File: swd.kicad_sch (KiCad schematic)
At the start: 3 parts, among them J2 ARM JTAG, U1 STM32H753ZIT6

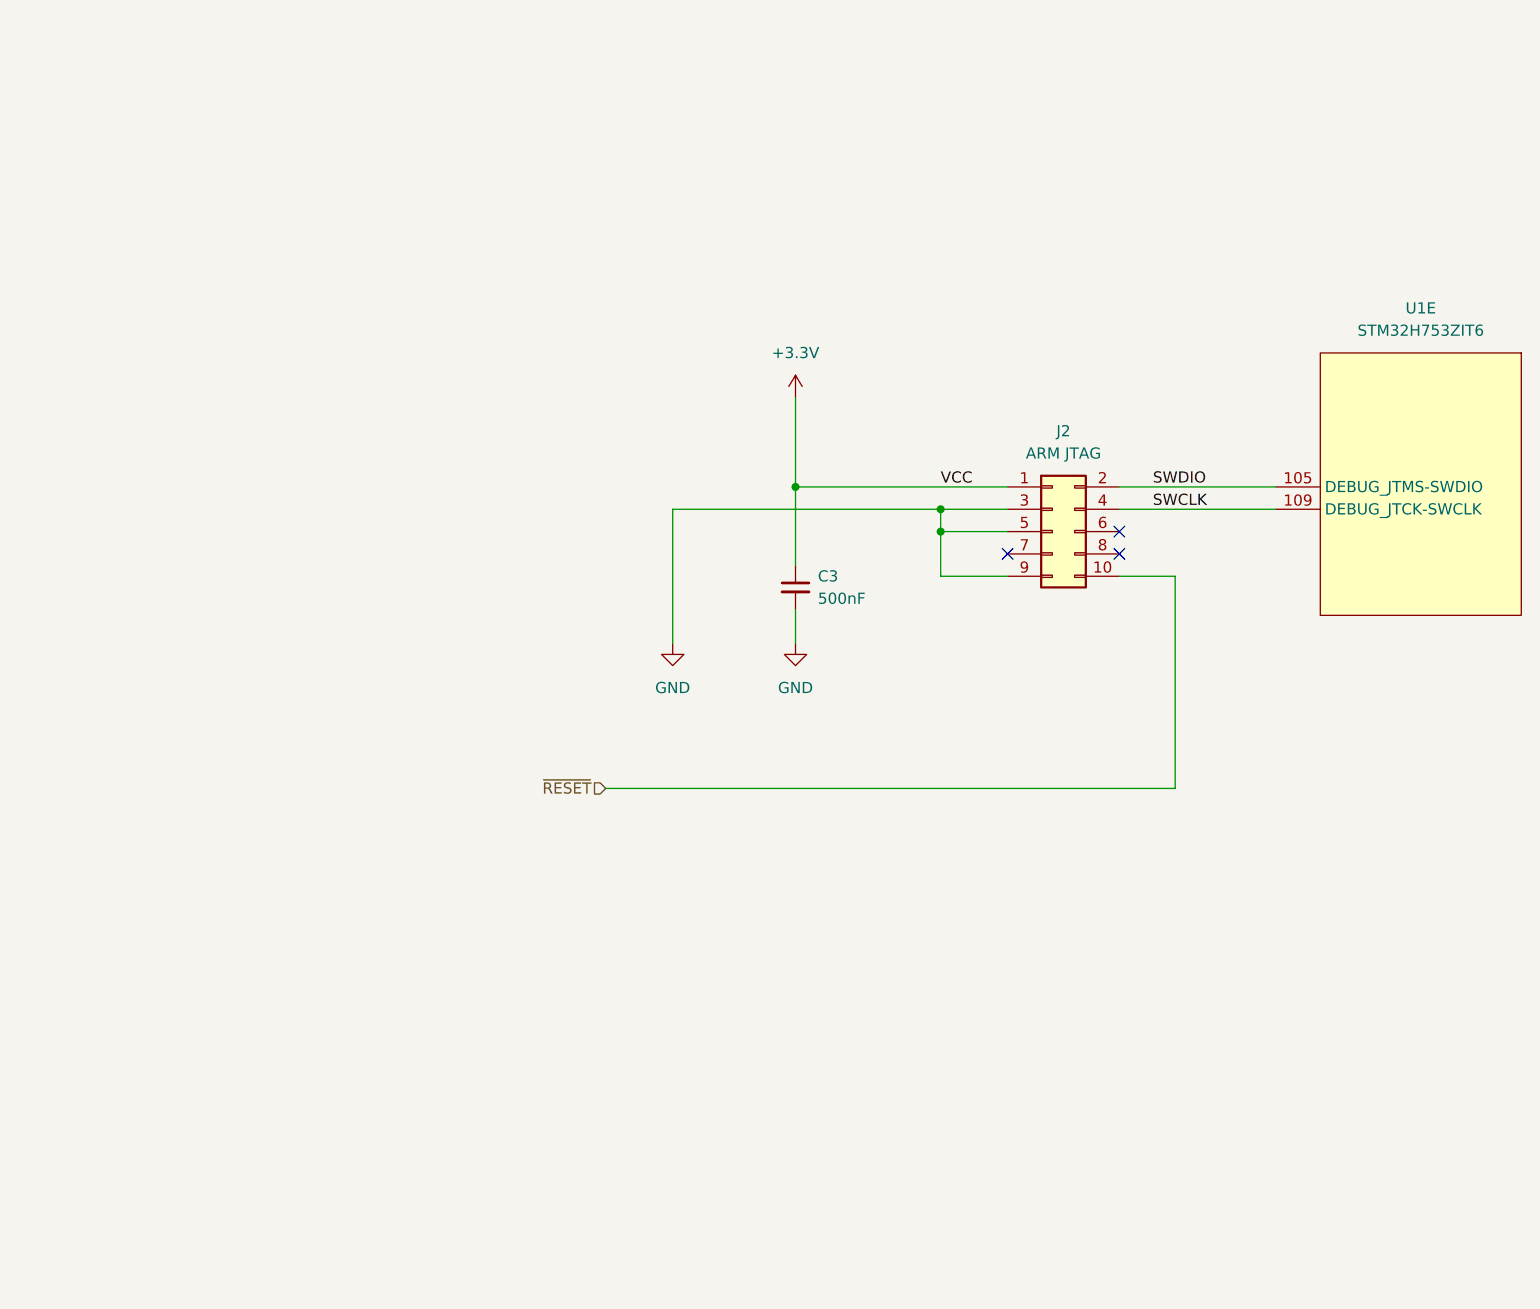
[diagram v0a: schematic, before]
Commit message: add SDIO
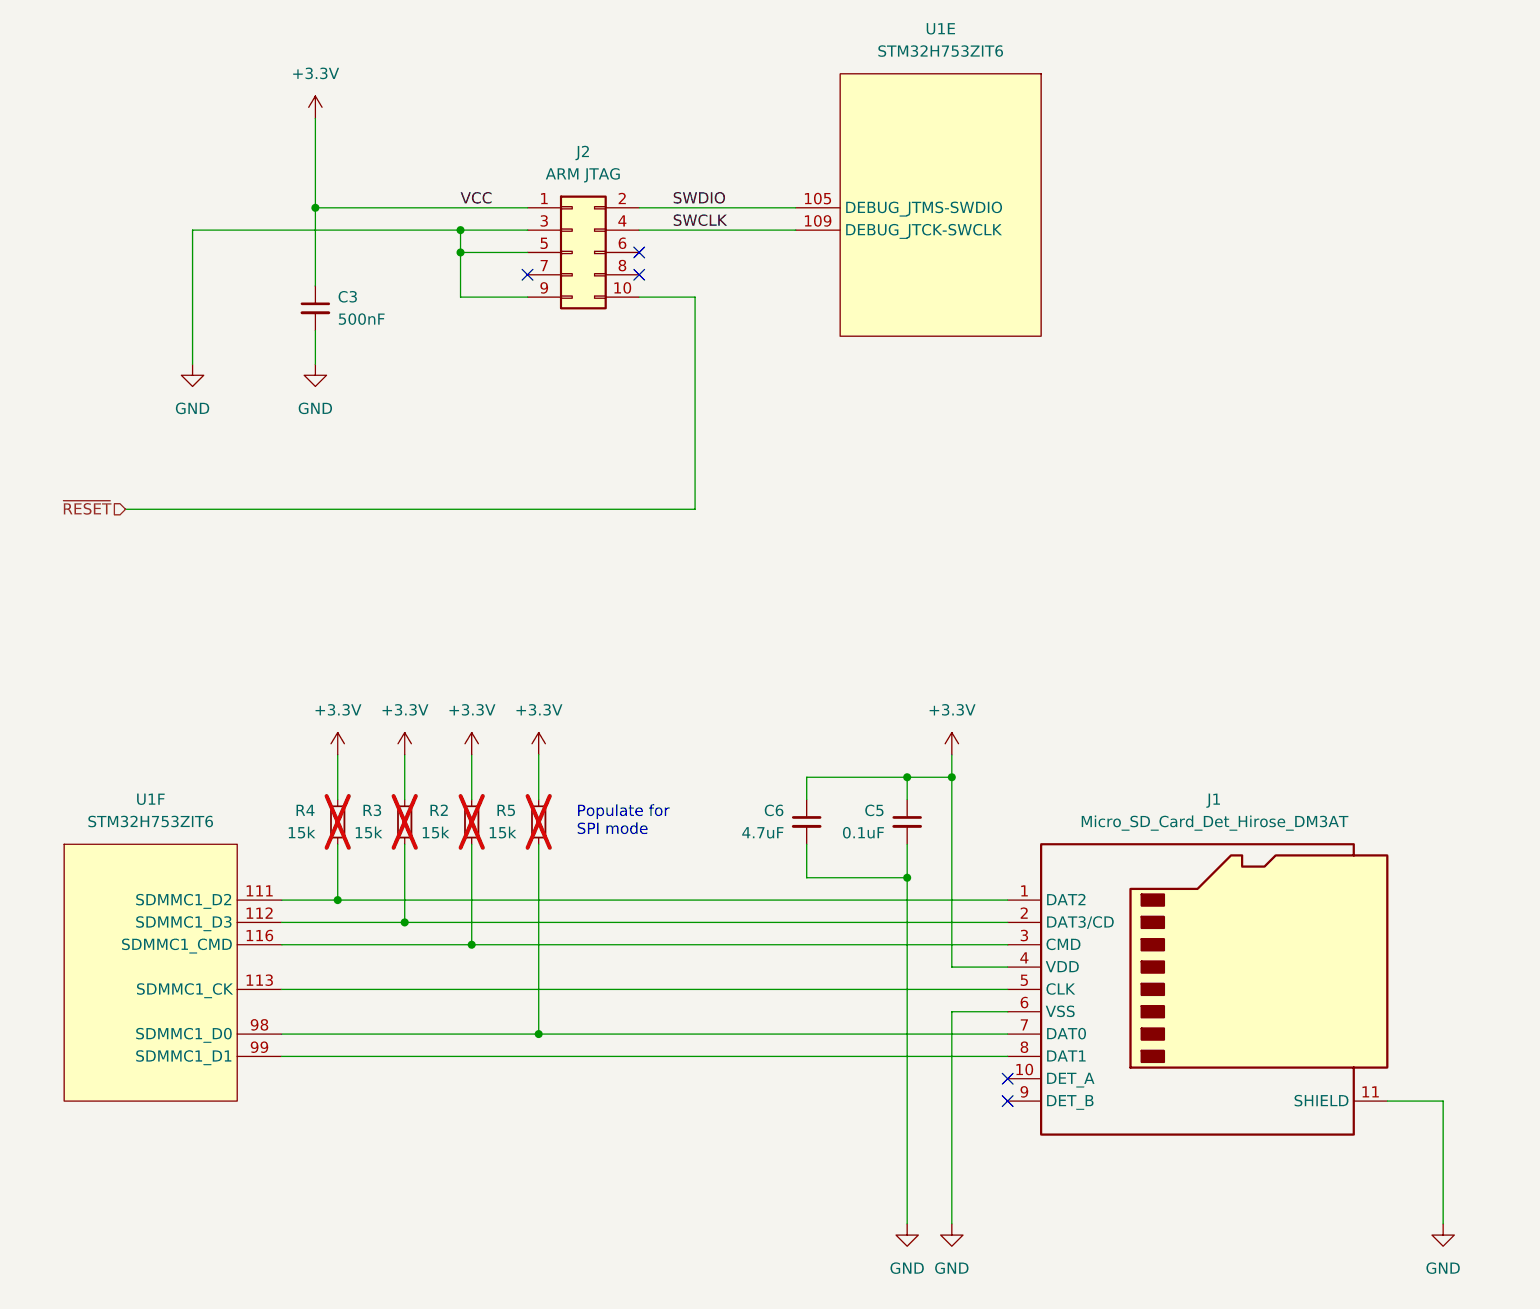
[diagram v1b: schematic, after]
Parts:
- added C5: 0.1uF, Capacitor_SMD:C_0402_1005Metric, symbol Device:C_Small
- added C6: 4.7uF, Capacitor_SMD:C_0805_2012Metric, symbol Device:C_Small
- added J1: Micro_SD_Card_Det_Hirose_DM3AT, Connector_Card:microSD_HC_Hirose_DM3AT-SF-PEJM5, symbol Connector:Micro_SD_Card_Det_Hirose_DM3AT
- added R2, R3, R4, R5: 15k, Resistor_SMD:R_0402_1005Metric, symbol Device:R_Small
- added unit 6 of U1
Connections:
- net +3.3V: now also C5.1, C6.1, J1.4 (VDD), R2.1, R3.1, R4.1, R5.1
- net GND: now also C5.2, C6.2, J1.11 (SHIELD), J1.6 (VSS)
- new net: J1.1 (DAT2), R4.2, U1.111 (SDMMC1_D2)
- new net: J1.2 (DAT3/CD), R3.2, U1.112 (SDMMC1_D3)
- new net: J1.5 (CLK), U1.113 (SDMMC1_CK)
- new net: J1.3 (CMD), R2.2, U1.116 (SDMMC1_CMD)
- new net: J1.7 (DAT0), R5.2, U1.98 (SDMMC1_D0)
- new net: J1.8 (DAT1), U1.99 (SDMMC1_D1)
- no-connect marks 3 -> 5
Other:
- note added: "Populate for SPI mode"
- moved on the sheet: C3, J2, U1E

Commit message: checkpoint
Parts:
- added D5: GRN, Diode_SMD:D_0603_1608Metric, symbol Part-DB:APTD1608LZGCK
- added R13, R6: 15k, Resistor_SMD:R_0402_1005Metric, symbol Device:R_Small
- J2: footprint (none) -> Package_SO:SOIC-10_3.9x4.9mm_P1mm
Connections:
- net +3.3V: now also R6.1
- net GND: now also J1.10 (DET_A), D5.1 (K)
- net ~{CARD_DET}: now reaches J1.9 (DET_B)
- net ~{CARD_DET}: now also U1.110 (PA15), R6.2
- new net: D5.2 (A), R13.2
- new net CARD_ACT: R13.1, U1.117 (PD3)
- no-connect marks 5 -> 3
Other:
- moved on the sheet: C5, C6, J1, R2, R3, R4, R5
